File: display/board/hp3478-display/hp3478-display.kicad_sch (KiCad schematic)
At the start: 59 parts, among them J1 Header, J2 Header, U1 FT60F1x2, U2 SM16206, U3 74HC595, U4 74HC595

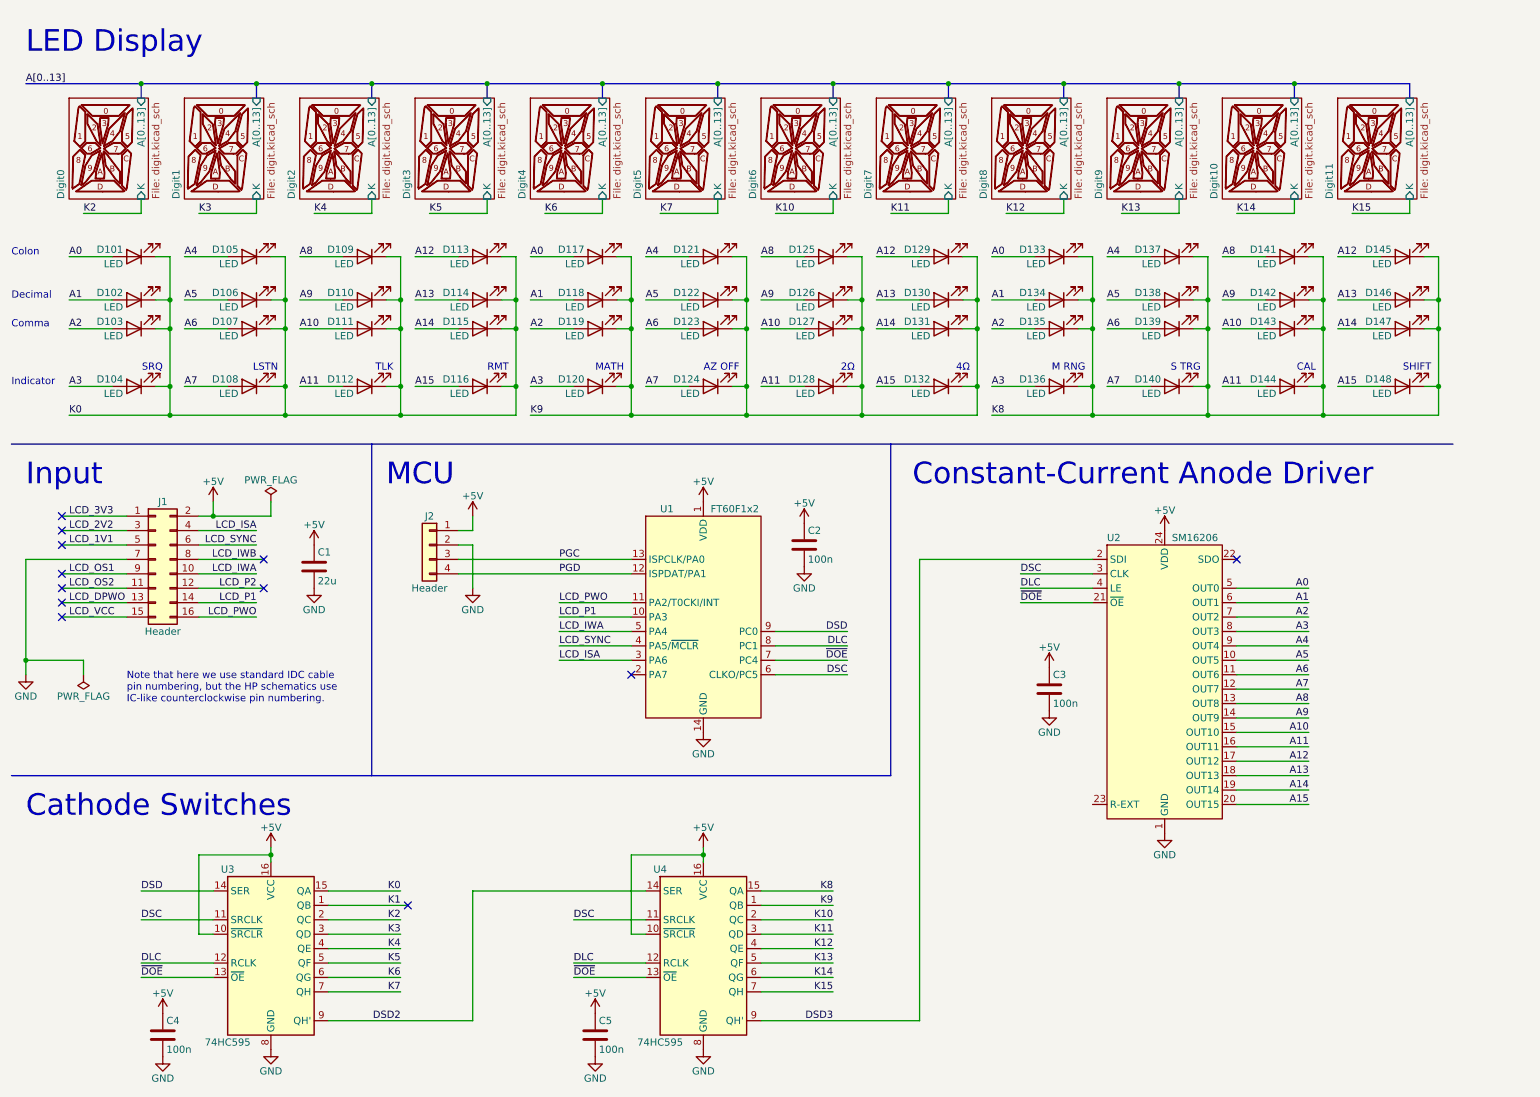
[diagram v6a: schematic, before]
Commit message: Swap anode and cathode - SM16206 is a low-side driver.
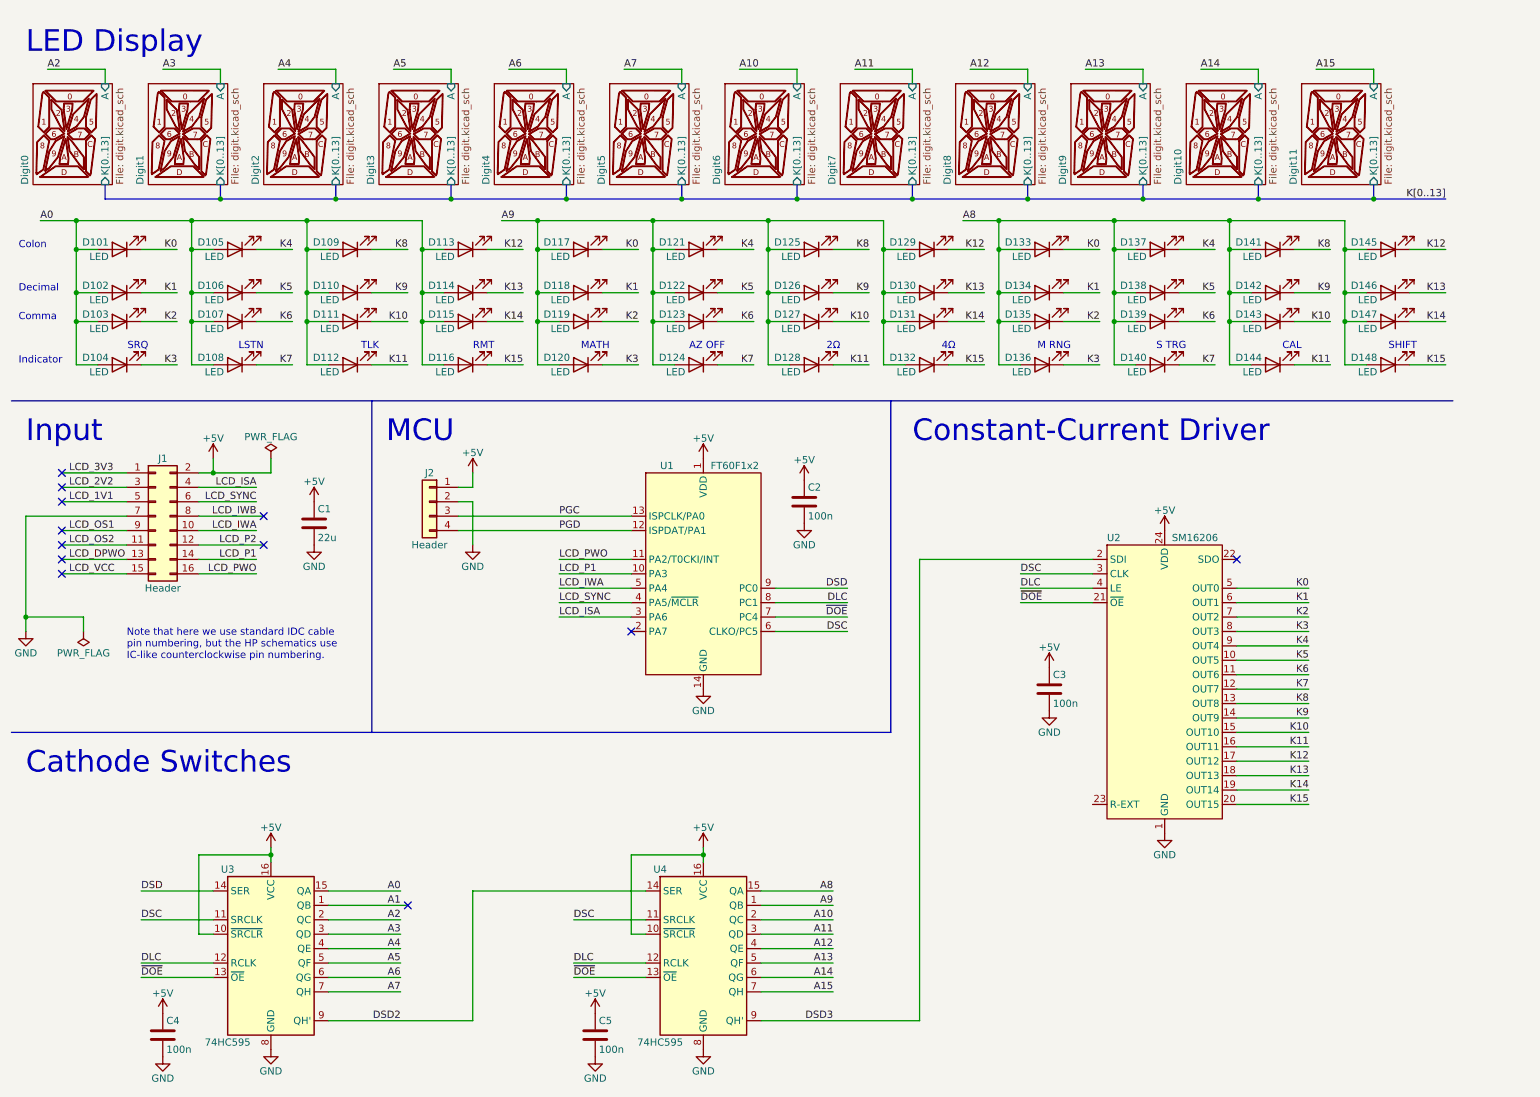
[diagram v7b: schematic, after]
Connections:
- net A0: now also D102.2 (A), D103.2 (A), D104.2 (A), D105.2 (A), D106.2 (A), D107.2 (A), D108.2 (A), D109.2 (A), D110.2 (A), D111.2 (A), D112.2 (A), D113.2 (A), D114.2 (A), D115.2 (A), D116.2 (A), U3.15 (QA); no longer D117.2 (A), D133.2 (A), U2.5 (OUT0)
- net A1: now also U3.1 (QB); no longer D102.2 (A), D118.2 (A), D134.2 (A), U2.6 (OUT1)
- net A10: now also U4.2 (QC); no longer D111.2 (A), D127.2 (A), D143.2 (A), U2.15 (OUT10)
- net A11: now also U4.3 (QD); no longer D112.2 (A), D128.2 (A), D144.2 (A), U2.16 (OUT11)
- net A12: now also U4.4 (QE); no longer D113.2 (A), D129.2 (A), D145.2 (A), U2.17 (OUT12)
- net A13: now also U4.5 (QF); no longer D114.2 (A), D130.2 (A), D146.2 (A), U2.18 (OUT13)
- net A14: now also U4.6 (QG); no longer D115.2 (A), D131.2 (A), D147.2 (A), U2.19 (OUT14)
- net A15: now also U4.7 (QH); no longer D116.2 (A), D132.2 (A), D148.2 (A), U2.20 (OUT15)
- net A2: now also U3.2 (QC); no longer D103.2 (A), D119.2 (A), D135.2 (A), U2.7 (OUT2)
- net A3: now also U3.3 (QD); no longer D104.2 (A), D120.2 (A), D136.2 (A), U2.8 (OUT3)
- net A4: now also U3.4 (QE); no longer D105.2 (A), D121.2 (A), D137.2 (A), U2.9 (OUT4)
- net A5: now also U3.5 (QF); no longer D106.2 (A), D122.2 (A), D138.2 (A), U2.10 (OUT5)
- net A6: now also U3.6 (QG); no longer D107.2 (A), D123.2 (A), D139.2 (A), U2.11 (OUT6)
- net A7: now also U3.7 (QH); no longer D108.2 (A), D124.2 (A), D140.2 (A), U2.12 (OUT7)
- net A8: now also D133.2 (A), D134.2 (A), D135.2 (A), D136.2 (A), D137.2 (A), D138.2 (A), D139.2 (A), D140.2 (A), D142.2 (A), D143.2 (A), D144.2 (A), D145.2 (A), D146.2 (A), D147.2 (A), D148.2 (A), U4.15 (QA); no longer D109.2 (A), D125.2 (A), U2.13 (OUT8)
- net A9: now also D117.2 (A), D118.2 (A), D119.2 (A), D120.2 (A), D121.2 (A), D122.2 (A), D123.2 (A), D124.2 (A), D125.2 (A), D127.2 (A), D128.2 (A), D129.2 (A), D130.2 (A), D131.2 (A), D132.2 (A), U4.1 (QB); no longer D110.2 (A), D142.2 (A), U2.14 (OUT9)
- net K0: now also D117.1 (K), D133.1 (K), U2.5 (OUT0); no longer D102.1 (K), D103.1 (K), D104.1 (K), D105.1 (K), D106.1 (K), D107.1 (K), D108.1 (K), D109.1 (K), D110.1 (K), D111.1 (K), D112.1 (K), D113.1 (K), D114.1 (K), D115.1 (K), D116.1 (K), U3.15 (QA)
- net K1: now also D102.1 (K), D118.1 (K), D134.1 (K), U2.6 (OUT1); no longer U3.1 (QB)
- net K10: now also D111.1 (K), D127.1 (K), D143.1 (K), U2.15 (OUT10); no longer U4.2 (QC)
- net K11: now also D112.1 (K), D128.1 (K), D144.1 (K), U2.16 (OUT11); no longer U4.3 (QD)
- net K12: now also D113.1 (K), D129.1 (K), D145.1 (K), U2.17 (OUT12); no longer U4.4 (QE)
- net K13: now also D114.1 (K), D130.1 (K), D146.1 (K), U2.18 (OUT13); no longer U4.5 (QF)
- net K14: now also D115.1 (K), D131.1 (K), D147.1 (K), U2.19 (OUT14); no longer U4.6 (QG)
- net K15: now also D116.1 (K), D132.1 (K), D148.1 (K), U2.20 (OUT15); no longer U4.7 (QH)
- net K2: now also D103.1 (K), D119.1 (K), D135.1 (K), U2.7 (OUT2); no longer U3.2 (QC)
- net K3: now also D104.1 (K), D120.1 (K), D136.1 (K), U2.8 (OUT3); no longer U3.3 (QD)
- net K4: now also D105.1 (K), D121.1 (K), D137.1 (K), U2.9 (OUT4); no longer U3.4 (QE)
- net K5: now also D106.1 (K), D122.1 (K), D138.1 (K), U2.10 (OUT5); no longer U3.5 (QF)
- net K6: now also D107.1 (K), D123.1 (K), D139.1 (K), U2.11 (OUT6); no longer U3.6 (QG)
- net K7: now also D108.1 (K), D124.1 (K), D140.1 (K), U2.12 (OUT7); no longer U3.7 (QH)
- net K8: now also D109.1 (K), D125.1 (K), U2.13 (OUT8); no longer D133.1 (K), D134.1 (K), D135.1 (K), D136.1 (K), D137.1 (K), D138.1 (K), D139.1 (K), D140.1 (K), D142.1 (K), D143.1 (K), D144.1 (K), D145.1 (K), D146.1 (K), D147.1 (K), D148.1 (K), U4.15 (QA)
- net K9: now also D110.1 (K), D142.1 (K), U2.14 (OUT9); no longer D117.1 (K), D118.1 (K), D119.1 (K), D120.1 (K), D121.1 (K), D122.1 (K), D123.1 (K), D124.1 (K), D125.1 (K), D127.1 (K), D128.1 (K), D129.1 (K), D130.1 (K), D131.1 (K), D132.1 (K), U4.1 (QB)
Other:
- sheet Digit0 ports: added A, K[0..13]; removed A[0..13], K
- sheet Digit1 ports: added A, K[0..13]; removed A[0..13], K
- sheet Digit10 ports: added A, K[0..13]; removed A[0..13], K
- sheet Digit11 ports: added A, K[0..13]; removed A[0..13], K
- sheet Digit2 ports: added A, K[0..13]; removed A[0..13], K
- sheet Digit3 ports: added A, K[0..13]; removed A[0..13], K
- sheet Digit4 ports: added A, K[0..13]; removed A[0..13], K
- sheet Digit5 ports: added A, K[0..13]; removed A[0..13], K
- sheet Digit6 ports: added A, K[0..13]; removed A[0..13], K
- sheet Digit7 ports: added A, K[0..13]; removed A[0..13], K
- sheet Digit8 ports: added A, K[0..13]; removed A[0..13], K
- sheet Digit9 ports: added A, K[0..13]; removed A[0..13], K
- note added: "Constant-Current Driver"
- note removed: "Constant-Current Anode Driver"
- moved on the sheet: C1, C2, D101, D102, D103, D104, D105, D106, D107, D108, D109, D110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

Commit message: Choose LEDs and set drive current.
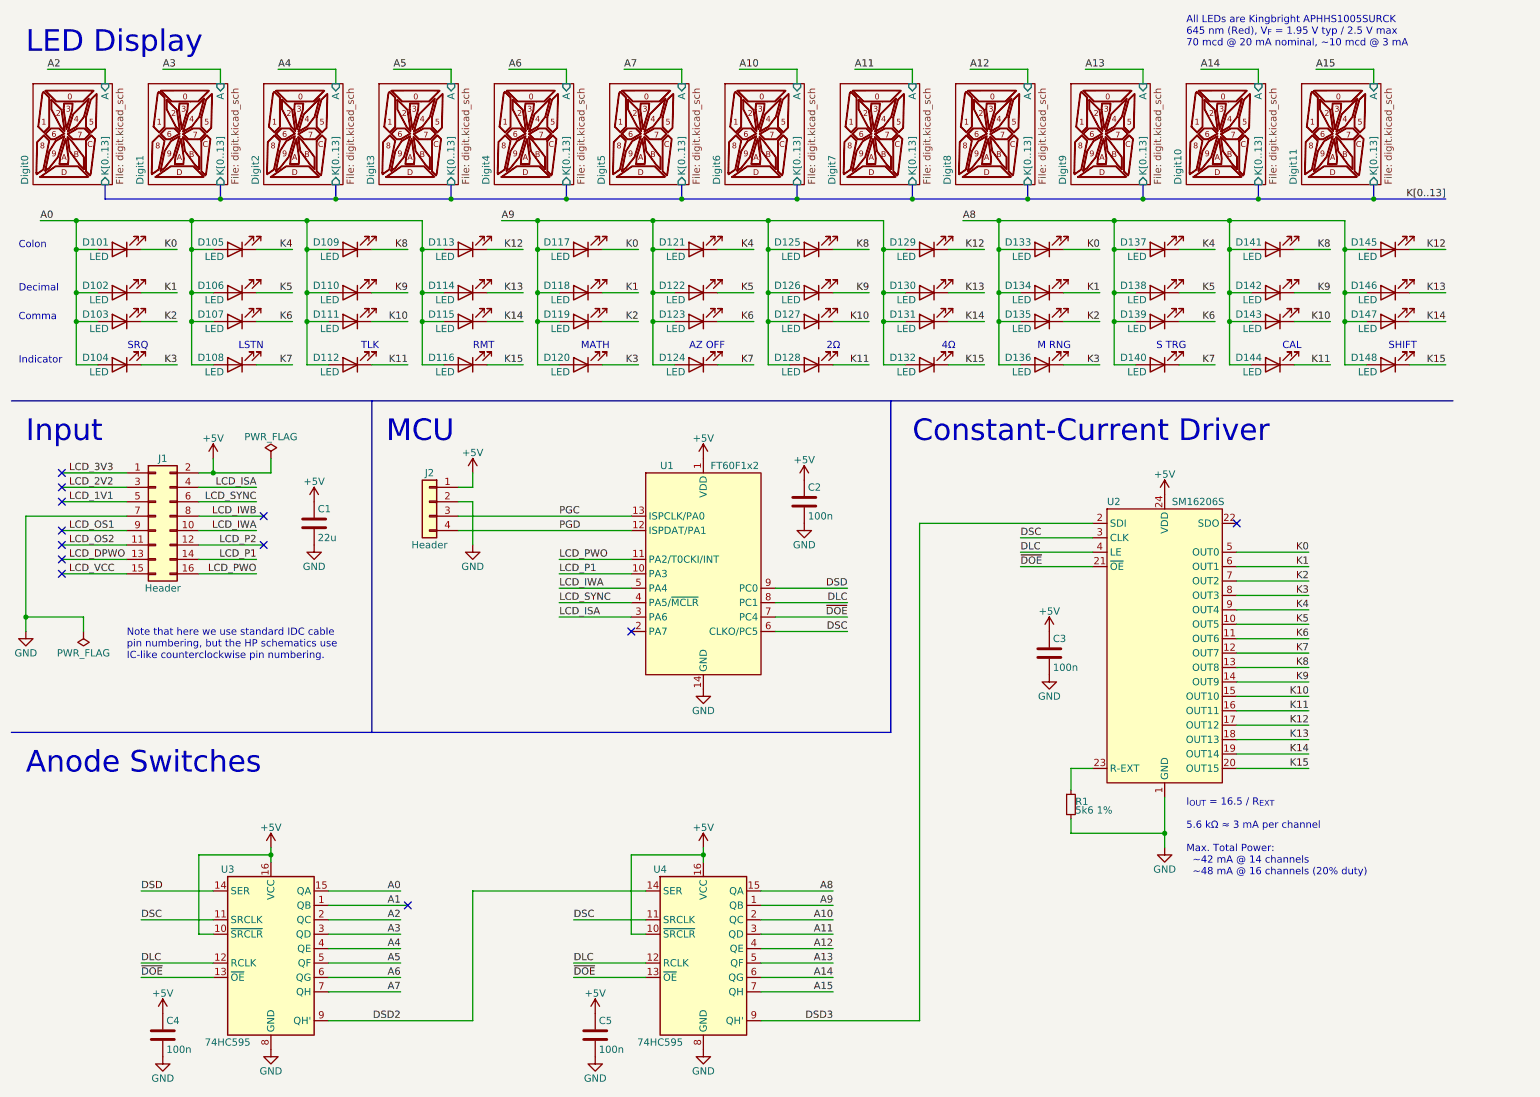
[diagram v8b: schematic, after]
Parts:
- added R1: 5k6 1%, Resistor_SMD:R_0603_1608Metric, symbol Device:R_Small
- D101, D102, D103, D104, D105, D106, D107, D108, D109, D110, D111, D112, D113, D114, D115, D116, D117, D118, D119, D120, D121, D122, D123, D124, D125, D126, D127, D128, D129, D130, D131, D132, D133, D134, D135, D136, D137, D138, D139, D140, D141, D142, D143, D144, D145, D146, D147, D148: JLC (none) -> C2852592
- U1: JLC (none) -> C708785
- U2: value SM16206 -> SM16206S; JLC (none) -> C121618
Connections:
- net GND: now also R1.2
- net at U2.23 (R-EXT): now also R1.1
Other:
- note added: "All LEDs are Kingbright APHHS1005SURCK 645 nm (Red), V_{F} = 1.95 V typ / 2.5 V max 70 mcd @ 20 mA nominal, ~10 mcd @ 3 mA"
- note added: "Anode Switches"
- note added: "I_{OUT} = 16.5 / R_{EXT} 5.6 kΩ ≈ 3 mA per channel Max. Total Power: ~42 mA @ 14 channels ~48 mA @ 16 channels (20% duty)"
- note removed: "Cathode Switches"
- moved on the sheet: C3, U2
